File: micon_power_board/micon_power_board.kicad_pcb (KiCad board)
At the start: 2 copper layers, 55 x 45 mm, 24 parts, among them J1 Conn_01x02_Pin, J2 Conn_01x02_Pin, J3 Conn_01x02_Pin, J4 Conn_01x02_Pin, J5 Conn_01x02_Pin, J6 Conn_01x02_Pin, J7 Conn_01x02_Socket, U1 M78AR05-1

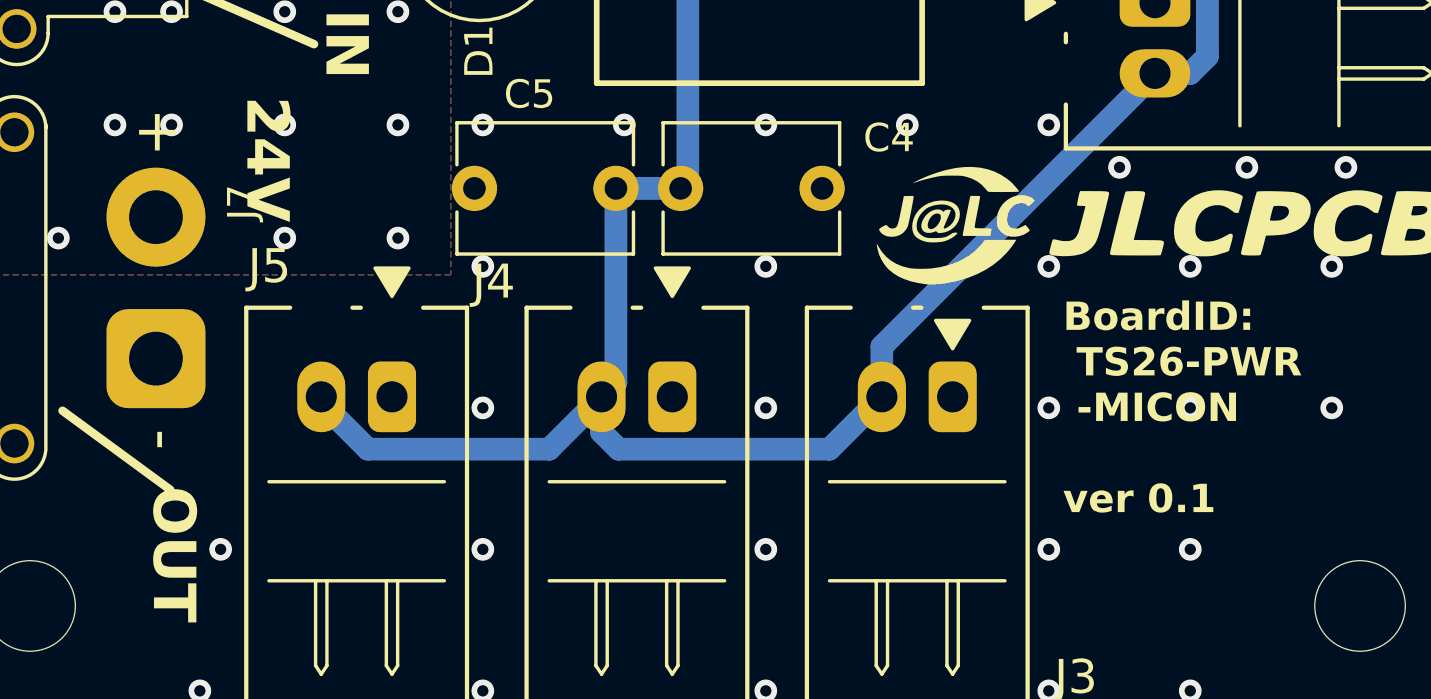
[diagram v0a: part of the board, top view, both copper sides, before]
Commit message: マイコン電源基板　シルクの重なりを修正，ver 0.2
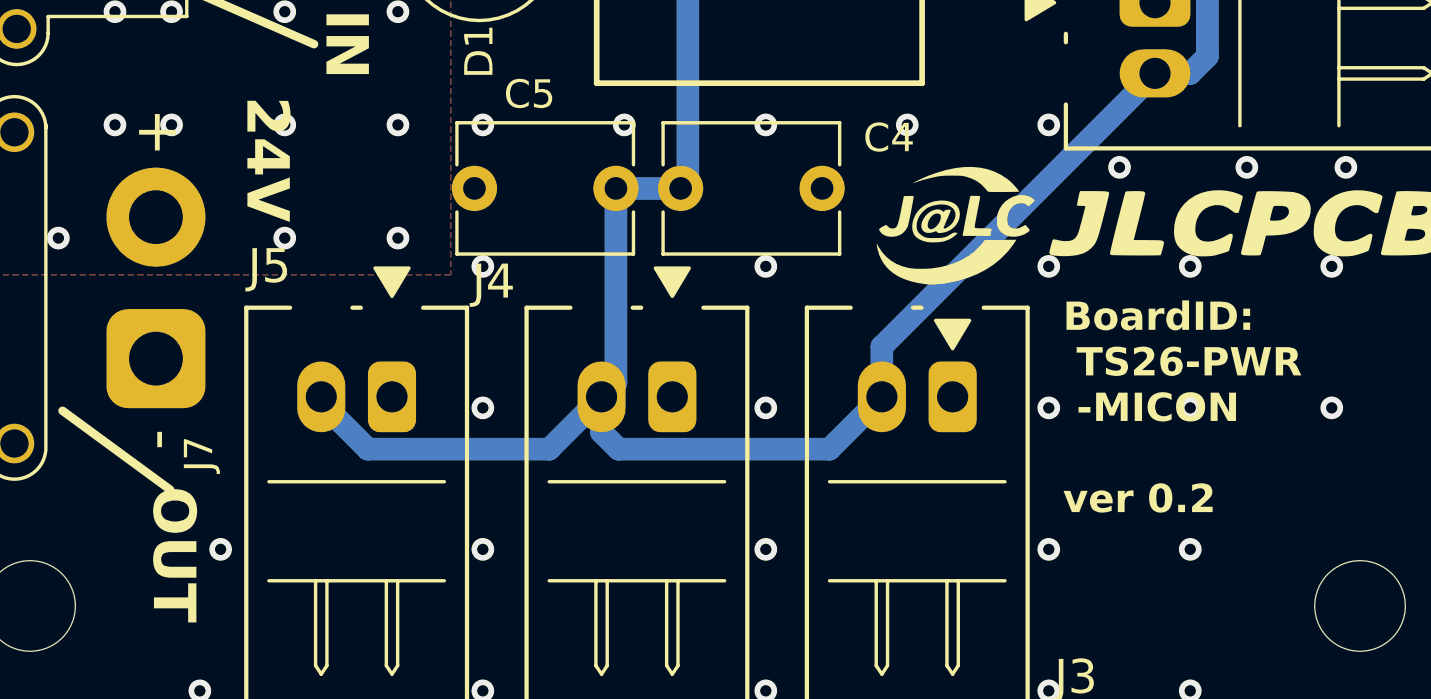
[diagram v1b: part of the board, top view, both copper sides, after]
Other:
- board text added: "BoardID: TS26-PWR -MICON ver 0.2"
- board text removed: "BoardID: TS26-PWR -MICON ver 0.1"
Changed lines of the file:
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@@
 		(tags "RC Connector XT30")
 		(property "Reference" "J7"
-			(at 5.524 3.048 90)
+			(at -3.366 1.524 90)
 			(layer "F.SilkS")
 			(effects
@@
 		(layer "Edge.Cuts")
 	)
-	(gr_text "BoardID:\n TS26-PWR\n -MICON\n\nver 0.1"
+	(gr_text "BoardID:\n TS26-PWR\n -MICON\n\nver 0.2"
 		(at 60.5 54 0)
 		(layer "F.SilkS")

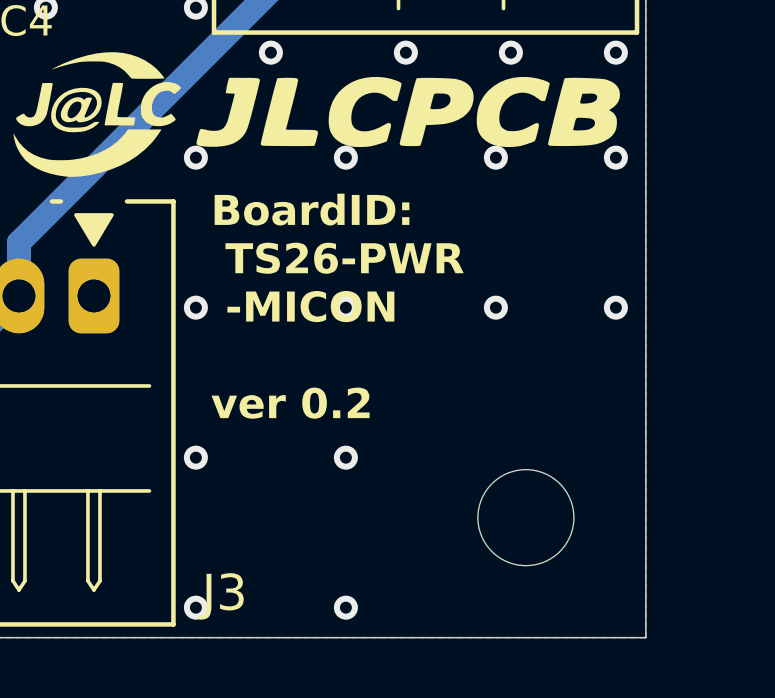
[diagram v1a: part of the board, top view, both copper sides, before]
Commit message: マイコン電源基板　岡ロボのシルクを追加，ver 0.3
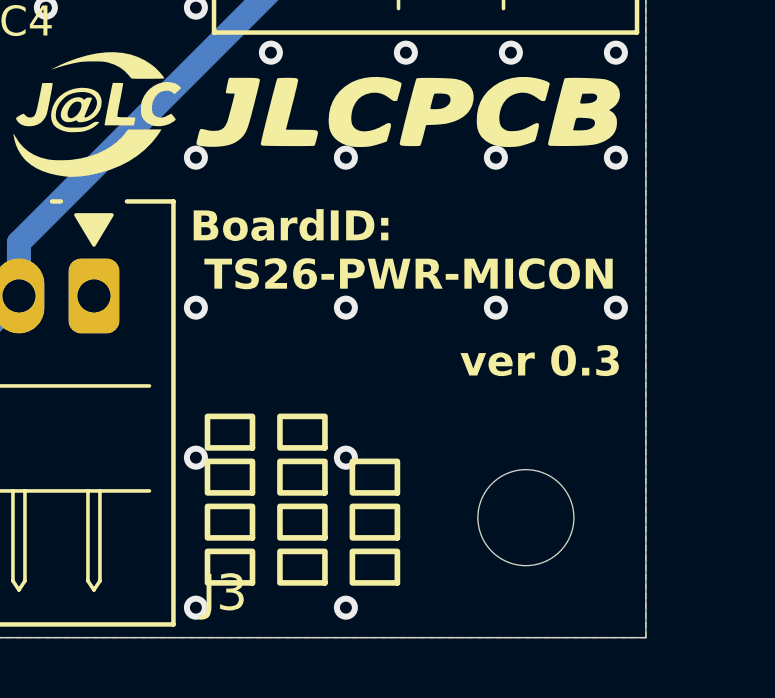
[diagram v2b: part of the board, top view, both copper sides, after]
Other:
- board text added: "BoardID: TS26-PWR-MICON"
- board text added: "ver 0.3"
- board text added: "岡山大学 ロボット 研究会"
- board text removed: "BoardID: TS26-PWR -MICON ver 0.2"
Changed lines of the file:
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@@
 		(layer "Edge.Cuts")
 	)
-	(gr_text "BoardID:\n TS26-PWR\n -MICON\n\nver 0.2"
-		(at 60.5 54 0)
+	(gr_text "BoardID:\n TS26-PWR-MICON"
+		(at 59.8 52.1 0)
 		(layer "F.SilkS")
 		(effects
@@
 		)
 	)
+	(gr_text "ver 0.3"
+		(at 68.8 55.8 0)
+		(layer "F.SilkS")
+		(effects
+			(font
+				(size 1 1)
+				(thickness 0.2)
+				(bold yes)
+			)
+			(justify left)
+		)
+	)
+	(gr_text "岡山大学\nロボット\n研究会"
+		(at 66.9 63.4 90)
+		(layer "F.SilkS")
+		(effects
+			(font
+				(size 1.5 1.5)
+				(thickness 0.1875)
+			)
+			(justify left bottom)
+		)
+	)

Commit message: マイコン電源基板　ナンバーのシルクを追加，ver0.4
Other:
- board text added: "No."
- board text added: "ver 0.4"
- board text removed: "ver 0.3"
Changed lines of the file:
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@@
+	)
+	(gr_rect
+		(start 66.55 34.1)
+		(end 73.45 46.6)
+		(stroke
+			(width 0.1)
+			(type solid)
+		)
+		(fill yes)
+		(layer "B.SilkS")
 	)
 	(gr_rect
@@
 		)
 	)
-	(gr_text "ver 0.3"
+	(gr_text "ver 0.4"
 		(at 68.8 55.8 0)
 		(layer "F.SilkS")
@@
 		)
 	)
+	(gr_text "No."
+		(at 73.3 28.9 90)
+		(layer "B.SilkS" knockout)
+		(effects
+			(font
+				(size 2 2)
+				(thickness 0.4)
+				(bold yes)
+			)
+			(justify left bottom mirror)
+		)
+	)

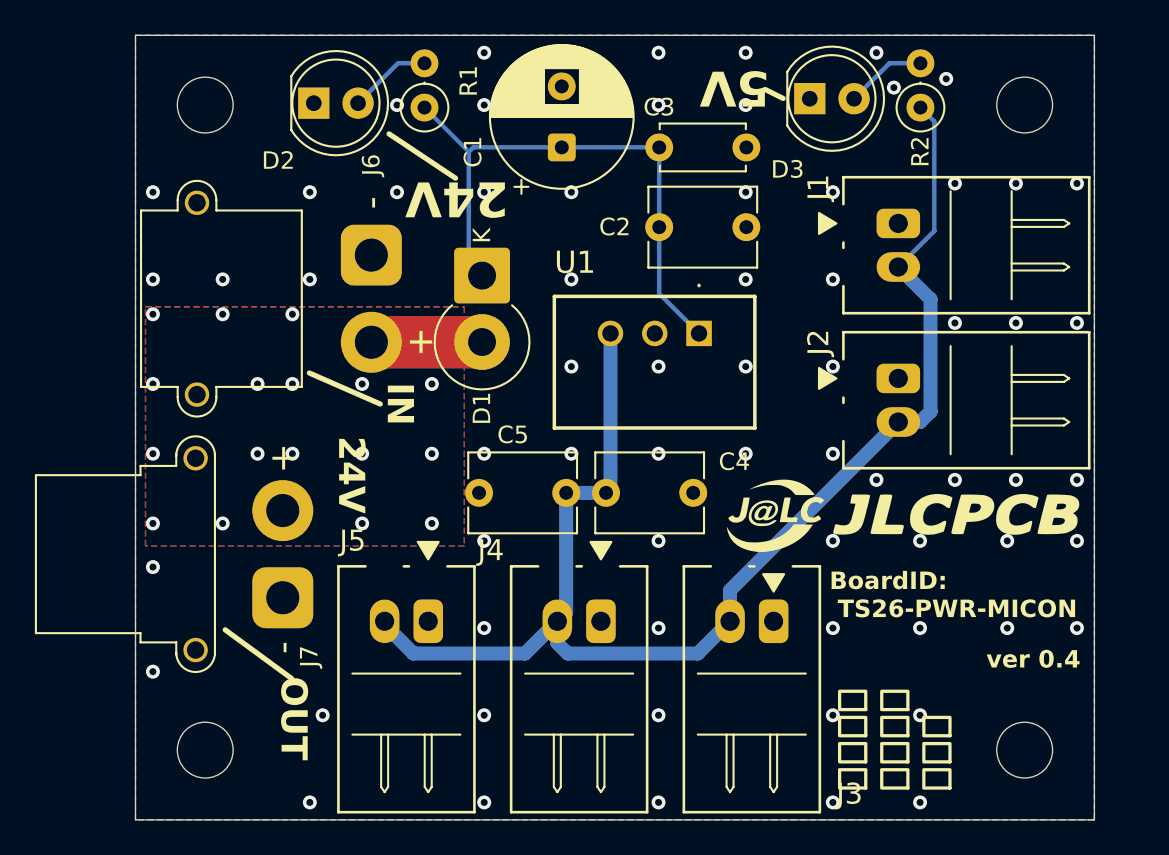
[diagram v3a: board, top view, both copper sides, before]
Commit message: マイコン電源基板　基板にテストポイントを追加，ver 0.5
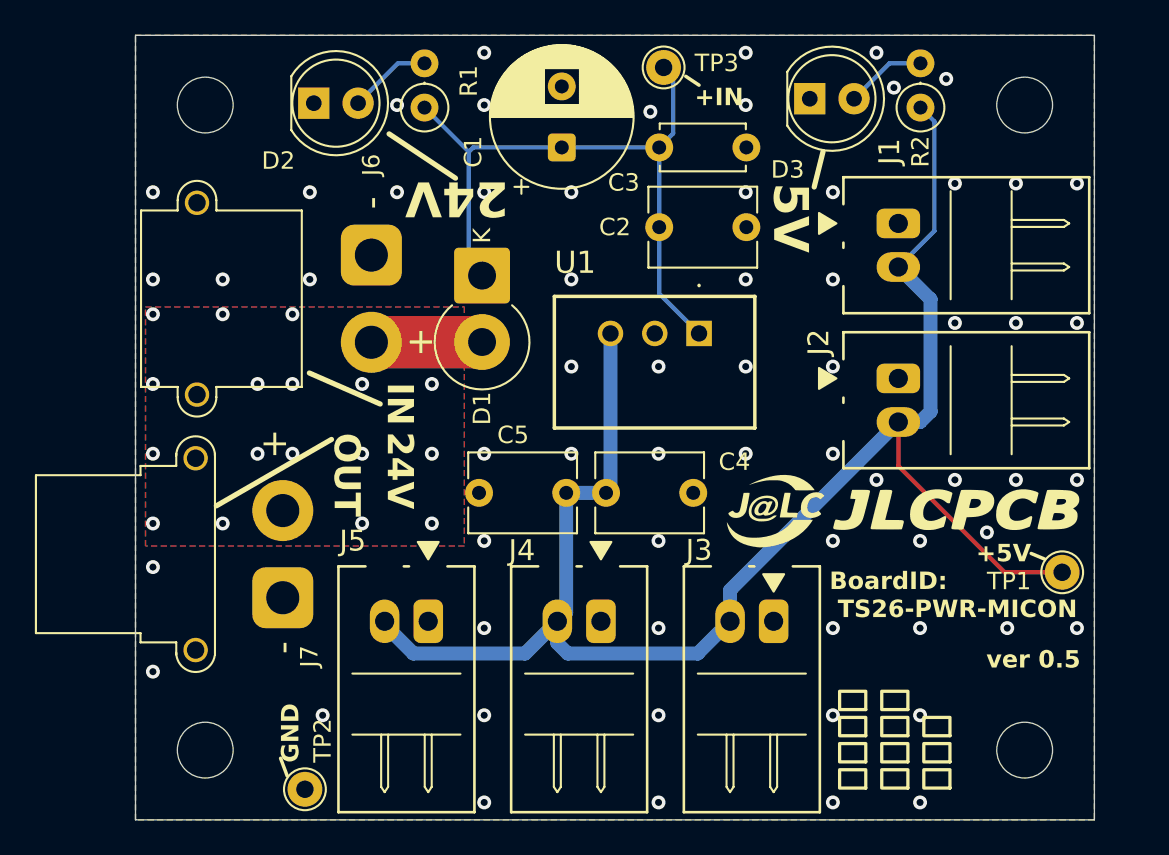
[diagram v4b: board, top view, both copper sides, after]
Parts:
- added TP1: TestPoint_Probe, TestPoint:TestPoint_THTPad_D2.0mm_Drill1.0mm, F.Cu at (73.2, 50.8)
- added TP2: TestPoint, TestPoint:TestPoint_THTPad_D2.0mm_Drill1.0mm, F.Cu at (29.7, 63.2)
- added TP3: TestPoint_Probe, TestPoint:TestPoint_THTPad_D2.0mm_Drill1.0mm, F.Cu at (50.3, 21.8)
- moved G*** 0.27 mm to (64.0, 47.2)
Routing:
- net Net-(J1-Pin_2): track 79.8 -> 94.2 mm
- net Net-(D1-K): track 33.6 -> 38.8 mm
- net GND: vias 66 -> 63
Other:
- board text added: "+5V"
- board text added: "+IN"
- board text added: "2026/09/24 Designed by E.Yoshioka"
- board text added: "GND"
- board text added: "ver 0.5"
- board text removed: "2026/09/20 Designed by E.Yoshioka"
- board text removed: "ver 0.4"
